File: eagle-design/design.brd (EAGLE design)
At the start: 83.8 x 51.7 mm, 19 parts, among them J1 61300411121, J2 10103594, U1 ATMEGA328P-AU

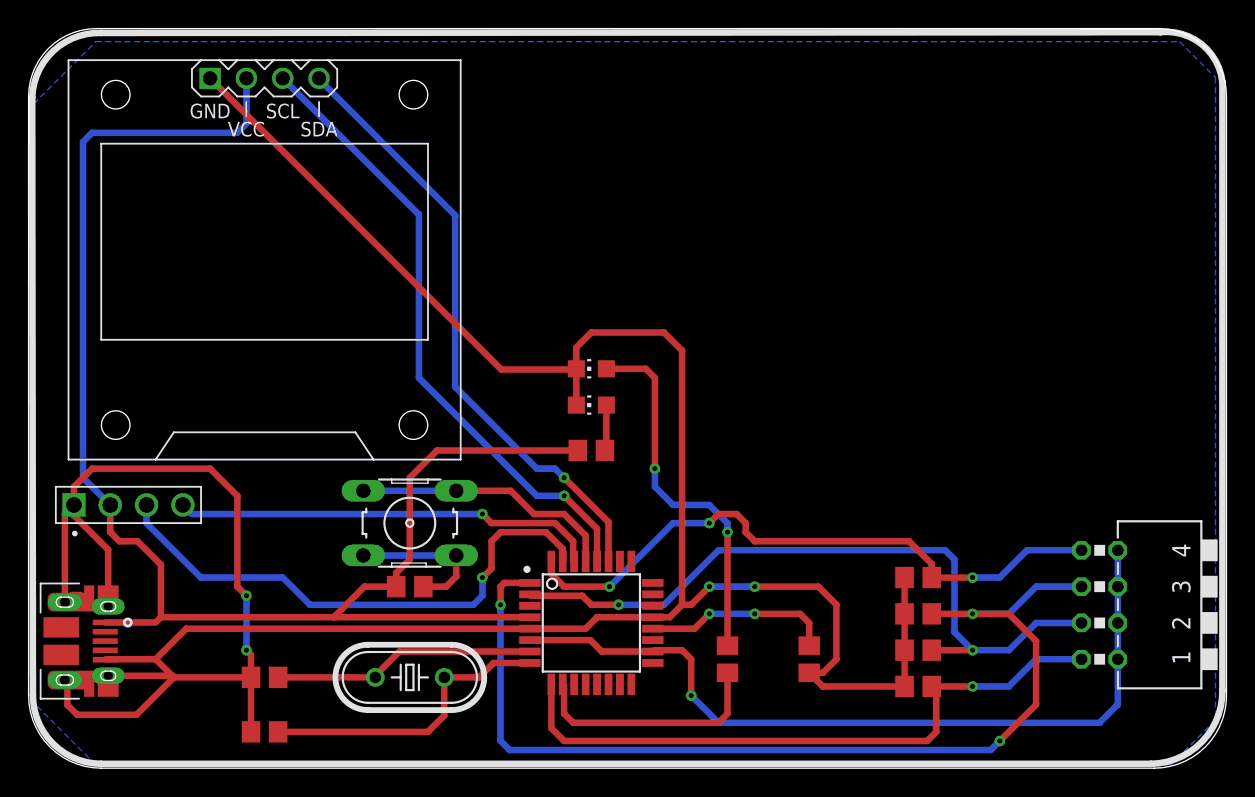
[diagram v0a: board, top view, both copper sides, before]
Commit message: Added ratsnet to top and bottom layer
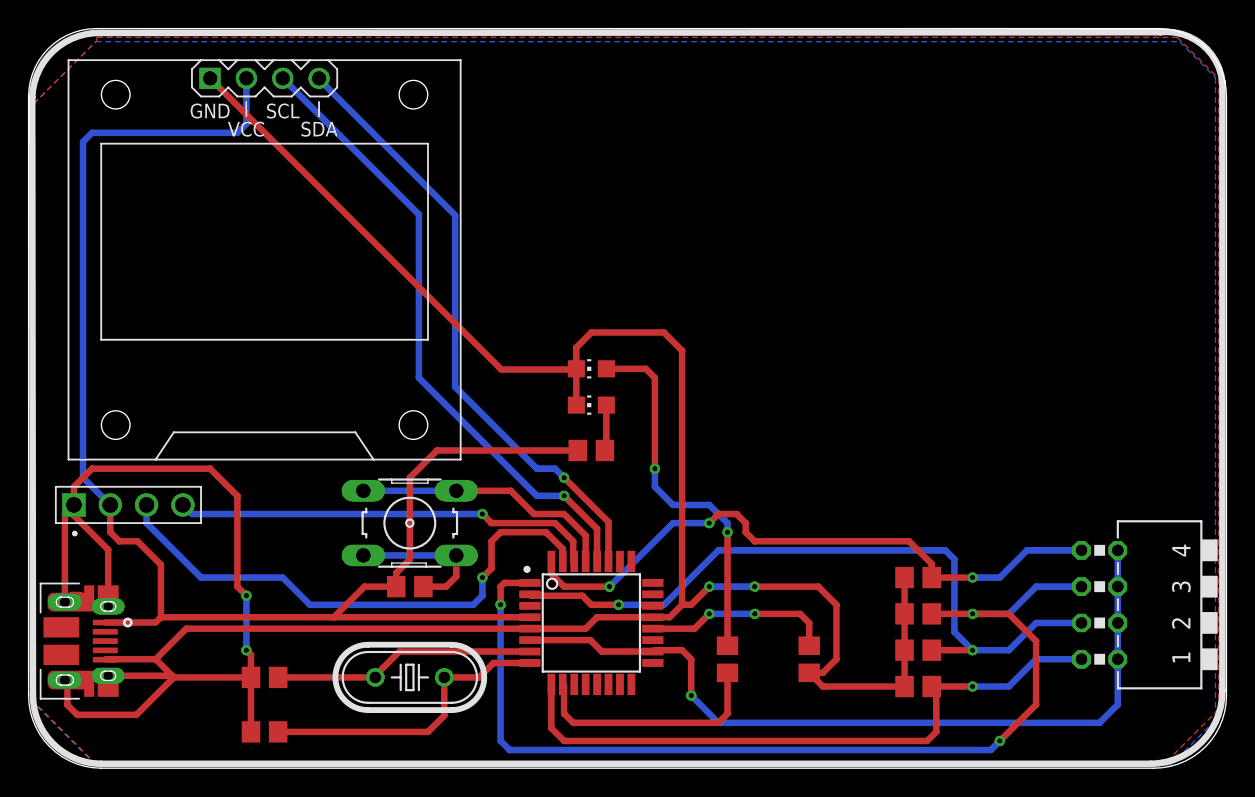
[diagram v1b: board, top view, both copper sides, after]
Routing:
- added copper zone on layer 1, net 5V
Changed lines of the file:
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@@
 <wire x1="16.9164" y1="45.3644" x2="17.5514" y2="45.9994" width="0.4572" layer="16"/>
 <wire x1="17.5514" y1="45.9994" x2="17.5514" y2="49.1744" width="0.4572" layer="16"/>
-<wire x1="37.3814" y1="11.4744" x2="37.3814" y2="9.8744" width="0" layer="19" extent="1-1"/>
+<polygon width="0.4572" layer="1">
+<vertex x="2.667" y="47.3964"/>
+<vertex x="7.0866" y="51.816"/>
+<vertex x="7.0866" y="52.0446"/>
+<vertex x="82.677" y="52.0446"/>
+<vertex x="85.5726" y="49.149"/>
+<vertex x="85.5726" y="5.0292"/>
+<vertex x="81.6864" y="1.143"/>
+<vertex x="7.0866" y="1.143"/>
+<vertex x="2.5908" y="5.6388"/>
+<vertex x="2.5908" y="47.3202"/>
+</polygon>
 </signal>
 <signal name="TX">
